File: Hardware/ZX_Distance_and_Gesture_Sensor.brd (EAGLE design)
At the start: 55.9 x 12.7 mm, 48 parts, among them Q1 MMBT2222A, Q2 MOSFET-NCHANNEL2N7002PW, U1 BRM-2508VERT

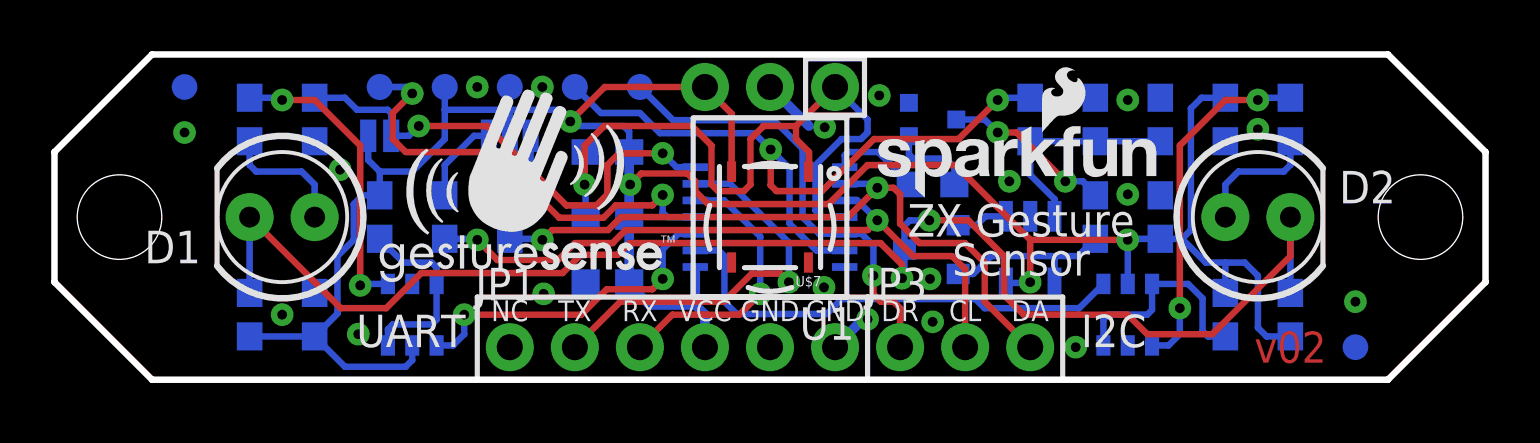
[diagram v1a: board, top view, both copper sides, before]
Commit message: Added solder tabs to blinders
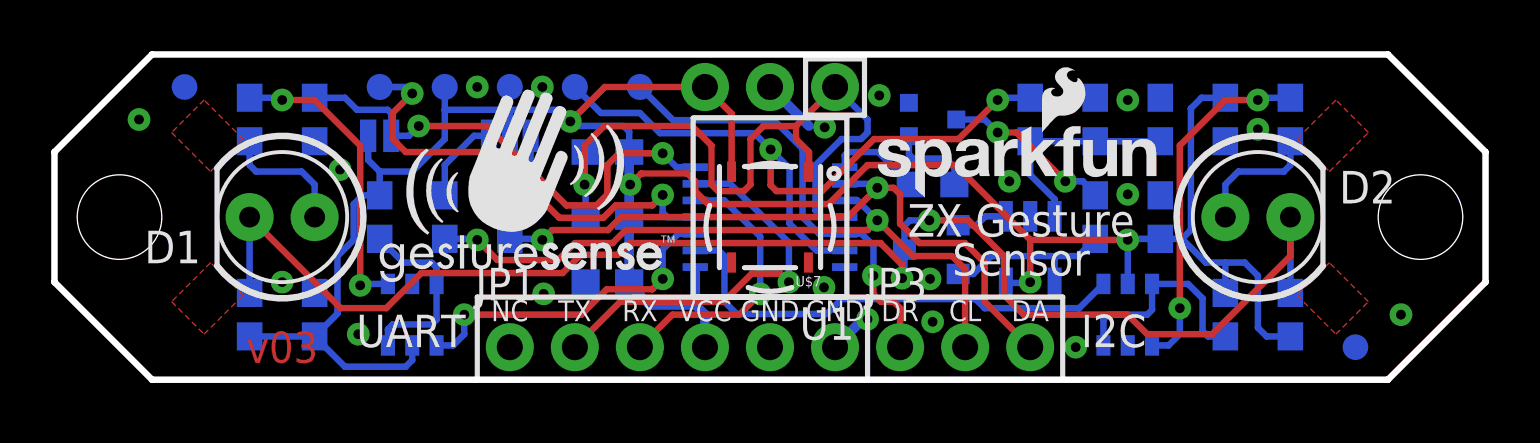
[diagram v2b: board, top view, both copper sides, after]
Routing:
- added copper zone on layer 1, net N$15
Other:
- board text added: "v03"
- board text removed: "v02"
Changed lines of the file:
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@@
 <setting verticaltext="up"/>
 </settings>
-<grid distance="0.05" unitdist="inch" unit="inch" style="dots" multiple="1" display="yes" altdistance="0.005" altunitdist="inch" altunit="inch"/>
+<grid distance="0.05" unitdist="inch" unit="inch" style="dots" multiple="1" display="yes" altdistance="0.025" altunitdist="inch" altunit="inch"/>
 <layers>
 <layer number="1" name="Top" color="4" fill="1" visible="yes" active="yes"/>
@@
 <layer number="54" name="bGND_GNDA" color="1" fill="9" visible="no" active="no"/>
 <layer number="56" name="wert" color="7" fill="1" visible="no" active="no"/>
+<layer number="57" name="tCAD" color="7" fill="1" visible="no" active="no"/>
 <layer number="91" name="Nets" color="2" fill="1" visible="no" active="no"/>
 <layer number="92" name="Busses" color="1" fill="1" visible="no" active="no"/>
@@
 <layer number="97" name="Info" color="7" fill="1" visible="no" active="no"/>
 <layer number="98" name="Guide" color="6" fill="1" visible="no" active="no"/>
+<layer number="99" name="SpiceOrder" color="7" fill="1" visible="no" active="no"/>
 <layer number="100" name="Muster" color="7" fill="1" visible="no" active="no"/>
 <layer number="101" name="Patch_Top" color="12" fill="4" visible="no" active="no"/>
@@
 <layer number="108" name="tplace-old" color="10" fill="1" visible="no" active="no"/>
 <layer number="109" name="ref-old" color="11" fill="1" visible="no" active="no"/>
+<layer number="110" name="fp0" color="7" fill="1" visible="no" active="yes"/>
+<layer number="111" name="LPC17xx" color="7" fill="1" visible="no" active="yes"/>
+<layer number="112" name="tSilk" color="7" fill="1" visible="no" active="yes"/>
 <layer number="116" name="Patch_BOT" color="9" fill="4" visible="no" active="no"/>
 <layer number="121" name="_tsilk" color="7" fill="1" visible="no" active="no"/>
 <layer number="122" name="_bsilk" color="7" fill="1" visible="no" active="no"/>
+<layer number="123" name="tTestmark" color="7" fill="1" visible="no" active="yes"/>
+<layer number="124" name="bTestmark" color="7" fill="1" visible="no" active="yes"/>
 <layer number="125" name="_tNames" color="7" fill="1" visible="no" active="no"/>
+<layer number="126" name="_bNames" color="7" fill="1" visible="no" active="yes"/>
+<layer number="127" name="_tValues" color="7" fill="1" visible="no" active="yes"/>
+<layer number="128" name="_bValues" color="7" fill="1" visible="no" active="yes"/>
+<layer number="131" name="tAdjust" color="7" fill="1" visible="no" active="yes"/>
+<layer number="132" name="bAdjust" color="7" fill="1" visible="no" active="yes"/>
 <layer number="144" name="Drill_legend" color="7" fill="1" visible="no" active="no"/>
+<layer number="150" name="Notes" color="7" fill="1" visible="no" active="yes"/>
 <layer number="151" name="HeatSink" color="7" fill="1" visible="no" active="no"/>
+<layer number="152" name="_bDocu" color="7" fill="1" visible="no" active="yes"/>
+<layer number="153" name="FabDoc1" color="7" fill="1" visible="no" active="yes"/>
+<layer number="154" name="FabDoc2" color="7" fill="1" visible="no" active="yes"/>
+<layer number="155" name="FabDoc3" color="7" fill="1" visible="no" active="yes"/>
 <layer number="199" name="Contour" color="7" fill="1" visible="no" active="no"/>
 <layer number="200" name="200bmp" color="1" fill="10" visible="no" active="no"/>
@@
 <layer number="223" name="223bmp" color="24" fill="1" visible="no" active="no"/>
 <layer number="224" name="224bmp" color="25" fill="1" visible="no" active="no"/>
+<layer number="248" name="Housing" color="7" fill="1" visible="no" active="yes"/>
+<layer number="249" name="Edge" color="7" fill="1" visible="no" active="yes"/>
 <layer number="250" name="Descript" color="3" fill="1" visible="no" active="no"/>
 <layer number="251" name="SMDround" color="12" fill="11" visible="no" active="no"/>
@@
 <text x="-13.3096" y="0.7366" size="0.8128" layer="22" font="vector" ratio="15" rot="MR270" align="bottom-center">I2C Addr</text>
 <text x="9.8044" y="-0.762" size="1.27" layer="21" font="vector" ratio="15" align="bottom-center">ZX Gesture</text>
-<text x="20.32" y="-5.08" size="1.2192" layer="1" font="vector" ratio="15" rot="R180" align="center">v02</text>
+<text x="-19.05" y="-5.08" size="1.2192" layer="1" font="vector" ratio="15" rot="R180" align="center">v03</text>
 <text x="-3.937" y="3.302" size="0.8128" layer="22" font="vector" ratio="15" rot="MR0" align="bottom-center">I2C Pullups</text>
 <dimension x1="24.13" y1="6.35" x2="24.13" y2="-6.35" x3="35.56" y3="0" textsize="1.778" textratio="15" layer="51" unit="inch"/>
@@
 <wire x1="11.43" y1="-3.1242" x2="11.43" y2="-6.35" width="0.2032" layer="21"/>
 <text x="9.8044" y="-2.286" size="1.27" layer="21" font="vector" ratio="15" align="bottom-center">Sensor</text>
+<circle x="19.05" y="0" radius="3.556" width="0.508" layer="51"/>
+<circle x="-19.05" y="0" radius="3.556" width="0.508" layer="51"/>
+<wire x1="19.05" y1="3.81" x2="22.86" y2="0" width="0.254" layer="51"/>
+<wire x1="22.86" y1="0" x2="19.05" y2="-3.81" width="0.254" layer="51"/>
+<wire x1="-22.86" y1="0" x2="-19.05" y2="-3.81" width="0.254" layer="51"/>
+<wire x1="-19.05" y1="3.81" x2="-22.86" y2="0" width="0.254" layer="51"/>
+<polygon width="0.254" layer="29">
+<vertex x="22.098" y="4.6736"/>
+<vertex x="23.4696" y="3.302"/>
+<vertex x="21.844" y="1.6764"/>
+<vertex x="20.4724" y="3.048"/>
+</polygon>
+<polygon width="0.254" layer="29">
+<vertex x="20.4724" y="-3.048"/>
+<vertex x="21.844" y="-1.6764"/>
+<vertex x="23.4696" y="-3.302"/>
+<vertex x="22.098" y="-4.6736"/>
+</polygon>
+<polygon width="0.254" layer="29">
+<vertex x="-21.844" y="-1.6764"/>
+<vertex x="-20.4724" y="-3.048"/>
+<vertex x="-22.098" y="-4.6736"/>
+<vertex x="-23.4696" y="-3.302"/>
+</polygon>
+<polygon width="0.254" layer="29">
+<vertex x="-23.4696" y="3.302"/>
+<vertex x="-22.098" y="4.6736"/>
+<vertex x="-20.4724" y="3.048"/>
+<vertex x="-21.844" y="1.6764"/>
+</polygon>
 </plain>
 <attributes>
@@
 <contactref element="TP2" pad="P$1"/>
 <contactref element="U1" pad="2"/>
-<polygon width="0.254" layer="1" isolate="0.2032">
+<polygon width="0.254" layer="1" isolate="0.2032" rank="5">
 <vertex x="-24.13" y="-6.35"/>
 <vertex x="24.13" y="-6.35"/>
@@
 </polygon>
 <via x="-16.7894" y="1.8542" extent="1-16" drill="0.381"/>
-<via x="-19.05" y="-3.81" extent="1-16" drill="0.381"/>
+<via x="-19.05" y="-2.54" extent="1-16" drill="0.381"/>
 <via x="6.2484" y="-2.413" extent="1-16" drill="0.381"/>
 <via x="6.35" y="-4.0894" extent="1-16" drill="0.381"/>
@@
 <via x="2.1336" y="3.5052" extent="1-16" drill="0.381"/>
 <wire x1="1.524" y1="3.556" x2="0" y2="5.08" width="0.381" layer="16"/>
-<via x="22.86" y="-3.302" extent="1-16" drill="0.381"/>
-<via x="-22.86" y="3.302" extent="1-16" drill="0.381"/>
+<via x="24.638" y="-3.81" extent="1-16" drill="0.381"/>
+<via x="-24.638" y="3.81" extent="1-16" drill="0.381"/>
 <via x="-8.89" y="5.08" extent="1-16" drill="0.381"/>
 <via x="-8.8392" y="-2.9972" extent="1-16" drill="0.381"/>
@@
 <signal name="N$14">
 </signal>
+<signal name="N$15">
+<polygon width="0.254" layer="1" isolate="0.3048" rank="2">
+<vertex x="20.574" y="3.048"/>
+<vertex x="21.844" y="1.778"/>
+<vertex x="23.368" y="3.302"/>
+<vertex x="22.098" y="4.572"/>
+</polygon>
+<polygon width="0.254" layer="1" isolate="0.3048" rank="2">
+<vertex x="22.098" y="-4.572"/>
+<vertex x="23.368" y="-3.302"/>
+<vertex x="21.844" y="-1.778"/>
+<vertex x="20.574" y="-3.048"/>
+</polygon>
+<polygon width="0.254" layer="1" isolate="0.3048" rank="2">
+<vertex x="-21.844" y="1.778"/>
+<vertex x="-20.574" y="3.048"/>
+<vertex x="-22.098" y="4.572"/>
+<vertex x="-23.368" y="3.302"/>
+</polygon>
+<polygon width="0.254" layer="1" isolate="0.3048" rank="2">
+<vertex x="-20.574" y="-3.048"/>
+<vertex x="-21.844" y="-1.778"/>
+<vertex x="-23.368" y="-3.302"/>
+<vertex x="-22.098" y="-4.572"/>
+</polygon>
+</signal>
 </signals>

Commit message: Added second option for SMT IR LEDs. Added solder pads for blinders.
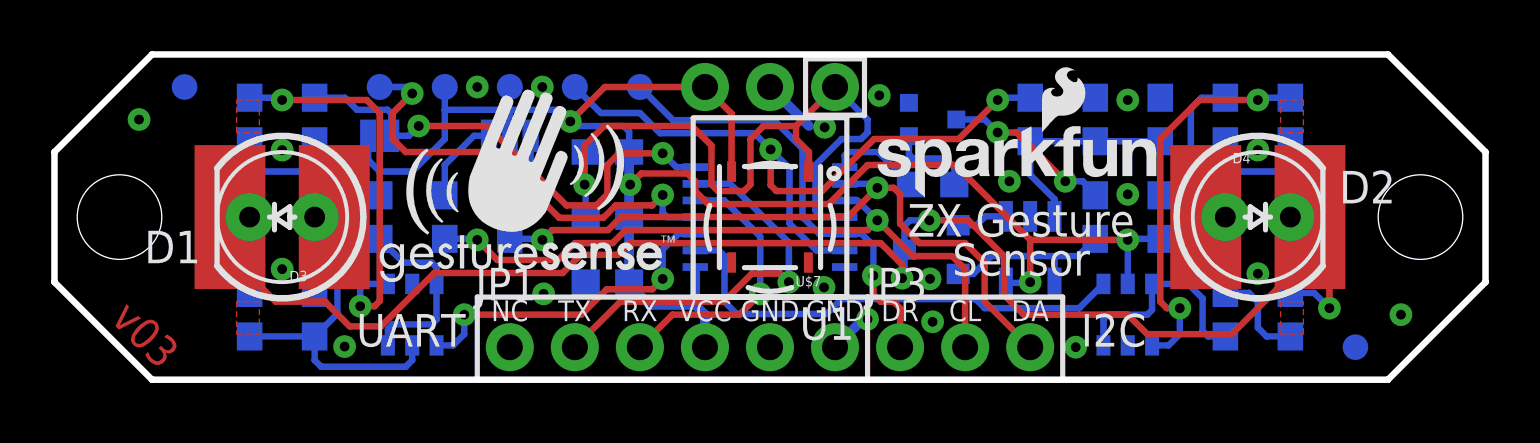
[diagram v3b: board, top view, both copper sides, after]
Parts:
- added D3, D4: SFH4641SHORT2, SparkFun-LED:SFH4641-SHORT2
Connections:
- net COMMON: now also D3.C, D4.C
- net N$12: now also D4.A
- net N$7: now also D3.A
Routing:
- net COMMON: track 57.6 -> 63.3 mm, vias 2 -> 3
- net N$6: track 11.7 -> 15.4 mm
- net N$11: track 13.7 -> 15.2 mm
- net VCC: track 96.0 -> 95.1 mm
- net N$7: track 5.05 -> 5.82 mm
- net N$12: track 5.05 -> 5.82 mm
- net GND: vias 19 -> 20
- added copper zone on layer 1, net N$16
- added copper zone on layer 1, net N$17
- added copper zone on layer 1, net N$18
